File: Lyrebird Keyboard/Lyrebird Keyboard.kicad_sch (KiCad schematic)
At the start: 99 parts, among them IC1 L7915CV, IC2 L78S15CV, IC3 MCP6022-E_SN, IC4 IR2113SPBF, IC5 IR2113SPBF, IC6 LM358DT, IC7 L7805ACD2T-TR, J1 WAV/ENV 4 (MIDI), J10 AC IN 2, J11 240V Out, J12 240 In, J13 Keys 1 to 14, J14 Keys 15 to 28, J15 Keys 29 to 33, J16 Keys 34 to 45, J17 Keys 46 to 59, J18 Keys 60 to 73, J19 Triangle Test, J2 WAV/ENV 3, J20 AMP Out, J21 SUB Out, J22 Square Test, J23 Bias Test Point 2, J24 Bias Test Point 1, J25 Pedals, J3 WAV/ENV 2, J4 WAV/ENV 1, J5 TONE SRC 4, J6 TONE SRC 3, J7 TONE SRC 2, J8 TONE SRC 1, J9 AC IN 1, Q1 BC848, Q2 BC848, Q3 IRFR2905ZTRPBF, Q4 IRFR2905ZTRPBF, Q5 IRFR2905ZTRPBF, Q6 IRFR2905ZTRPBF, U1 DF06S

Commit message: Mainboard Changes
Adjusted mainboard, the longer PCI slots are now instrument slots not wave shaper slots, and slot 4 in the longer is also able to support midi implementation
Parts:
- added C29, C30, C31, C32, C33, C34: T491A225K016AT, T491A, symbol SamacSys_Parts:T491A225K016AT
- J1: value WAV/ENV 4 (MIDI) -> INSTMNT 4 (MIDI)
- J15: value Keys 29 to 33 -> Keys 29 to 36
- J16: value Keys 34 to 45 -> Keys 37 to 45
- J2: value WAV/ENV 3 -> INSTMNT 3
- J3: value WAV/ENV 2 -> INSTMNT 2
- J4: value WAV/ENV 1 -> INSTMNT 1
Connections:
- net +15V: now also J1.A17, J1.A3, J1.B17, J1.B3, J2.A17, J2.A3, J2.B17, J2.B3, J3.A17, J3.A3, J3.B17, J3.B3, J4.A17, J4.A3, J4.B17, J4.B3, J5.A17, J5.A3, J5.B17, J5.B3, J6.A17, J6.A3, J6.B17, J6.B3, J7.A17, J7.A3, J7.B17, J7.B3, J8.A17, J8.A3, J8.B17, J8.B3; no longer J1.A18, J1.A4, J1.B18, J1.B4, J2.A18, J2.A4, J2.B18, J2.B4, J3.A18, J3.A4, J3.B18, J3.B4, J4.A18, J4.A4, J4.B18, J4.B4, J5.A18, J5.A4, J5.B18, J5.B4, J6.A18, J6.A4, J6.B18, J6.B4, J7.A18, J7.A4, J7.B18, J7.B4, J8.A18, J8.A4, J8.B18, J8.B4
- net +30V: now also J1.A1, J1.A15, J1.B1, J1.B15, J2.A1, J2.A15, J2.B1, J2.B15, J3.A1, J3.A15, J3.B1, J3.B15, J4.A1, J4.A15, J4.B1, J4.B15, J5.A1, J5.A15, J5.B1, J5.B15, J6.A1, J6.A15, J6.B1, J6.B15, J7.A1, J7.A15, J7.B1, J7.B15, J8.A1, J8.A15, J8.B1, J8.B15; no longer J1.A16, J1.A2, J1.B16, J1.B2, J2.A16, J2.A2, J2.B16, J2.B2, J3.A16, J3.A2, J3.B16, J3.B2, J4.A16, J4.A2, J4.B16, J4.B2, J5.A16, J5.A2, J5.B16, J5.B2, J6.A16, J6.A2, J6.B16, J6.B2, J7.A16, J7.A2, J7.B16, J7.B2, J8.A16, J8.A2, J8.B16, J8.B2
- net +5V: now also C29.1 (+), C30.1 (+), C31.1 (+), C32.1 (+), C33.1 (+), C34.1 (+)
- net +VED: now also J1.B7, J2.B7, J3.B7, J4.B7, J5.B7, J6.B7, J7.B7, J8.B7; no longer J1.B8, J2.B8, J3.B8, J4.B8, J5.B8, J6.B8, J7.B8, J8.B8
- net +VT: now also J1.A7, J2.A7, J3.A7, J4.A7, J5.A7, J6.A7, J7.A7, J8.A7; no longer J1.A8, J2.A8, J3.A8, J4.A8, J5.A8, J6.A8, J7.A8, J8.A8
- net -15V: now also J1.A19, J1.A5, J1.B19, J1.B5, J2.A19, J2.A5, J2.B19, J2.B5, J3.A19, J3.A5, J3.B19, J3.B5, J4.A19, J4.A5, J4.B19, J4.B5, J5.A19, J5.A5, J5.B19, J5.B5, J6.A19, J6.A5, J6.B19, J6.B5, J7.A19, J7.A5, J7.B19, J7.B5, J8.A19, J8.A5, J8.B19, J8.B5; no longer J1.A20, J1.A6, J1.B20, J1.B6, J2.A20, J2.A6, J2.B20, J2.B6, J3.A20, J3.A6, J3.B20, J3.B6, J4.A20, J4.A6, J4.B20, J4.B6, J5.A20, J5.A6, J5.B20, J5.B6, J6.A20, J6.A6, J6.B20, J6.B6, J7.A20, J7.A6, J7.B20, J7.B6, J8.A20, J8.A6, J8.B20, J8.B6
- net D#35: now also J15.9; no longer J16.5
- net D34: now also J15.8; no longer J16.6
- net E36: now also J15.10; no longer J16.8
- net EXP 1: now also J1.A33, J2.A33, J3.A33, J4.A33, J5.A33, J6.A33, J7.A33, J8.A33; no longer J1.A34, J2.A34, J3.A34, J4.A34, J5.A34, J6.A34, J7.A34, J8.A34
- net EXP 11: now also J1.B39, J2.B39, J3.B39, J4.B39, J5.B39, J6.B39, J7.B39, J8.B39; no longer J1.B40, J2.B40, J3.B40, J4.B40, J5.B40, J6.B40, J7.B40, J8.B40
- net EXP 12: now also J1.B41, J2.B41, J3.B41, J4.B41, J5.B41, J6.B41, J7.B41, J8.B41; no longer J1.B42, J2.B42, J3.B42, J4.B42, J5.B42, J6.B42, J7.B42, J8.B42
- net EXP 13: now also J1.B43, J2.B43, J3.B43, J4.B43, J5.B43, J6.B43, J7.B43, J8.B43; no longer J1.B44, J2.B44, J3.B44, J4.B44, J5.B44, J6.B44, J7.B44, J8.B44
- net EXP 2: now also J1.A35, J2.A35, J3.A35, J4.A35, J5.A35, J6.A35, J7.A35, J8.A35; no longer J1.A36, J2.A36, J3.A36, J4.A36, J5.A36, J6.A36, J7.A36, J8.A36
- net EXP 3: now also J1.A37, J2.A37, J3.A37, J4.A37, J5.A37, J6.A37, J7.A37, J8.A37; no longer J1.A38, J2.A38, J3.A38, J4.A38, J5.A38, J6.A38, J7.A38, J8.A38
- net EXP 4: now also J1.A39, J2.A39, J3.A39, J4.A39, J5.A39, J6.A39, J7.A39, J8.A39; no longer J1.A40, J2.A40, J3.A40, J4.A40, J5.A40, J6.A40, J7.A40, J8.A40
- net EXP 5: now also J1.A41, J2.A41, J3.A41, J4.A41, J5.A41, J6.A41, J7.A41, J8.A41; no longer J1.A42, J2.A42, J3.A42, J4.A42, J5.A42, J6.A42, J7.A42, J8.A42
- net EXP 6: now also J1.A43, J2.A43, J3.A43, J4.A43, J5.A43, J6.A43, J7.A43, J8.A43; no longer J1.A44, J2.A44, J3.A44, J4.A44, J5.A44, J6.A44, J7.A44, J8.A44
- net EXP 7: now also J1.A45, J2.A45, J3.A45, J4.A45, J5.A45, J6.A45, J7.A45, J8.A45; no longer J1.A46, J2.A46, J3.A46, J4.A46, J5.A46, J6.A46, J7.A46, J8.A46
- net EXP10: now also J1.B37, J2.B37, J3.B37, J4.B37, J5.B37, J6.B37, J7.B37, J8.B37; no longer J1.B38, J2.B38, J3.B38, J4.B38, J5.B38, J6.B38, J7.B38, J8.B38
- net EXP8: now also J1.B33, J2.B33, J3.B33, J4.B33, J5.B33, J6.B33, J7.B33, J8.B33; no longer J1.B34, J2.B34, J3.B34, J4.B34, J5.B34, J6.B34, J7.B34, J8.B34
- net EXP9: now also J1.B35, J2.B35, J3.B35, J4.B35, J5.B35, J6.B35, J7.B35, J8.B35; no longer J1.B36, J2.B36, J3.B36, J4.B36, J5.B36, J6.B36, J7.B36, J8.B36
- net GND: now also J1.A10, J1.A12, J1.A14, J1.A16, J1.A18, J1.A2, J1.A20, J1.A22, J1.A24, J1.A26, J1.A28, J1.A30, J1.A32, J1.A34, J1.A36, J1.A38, J1.A4, J1.A40, J1.A42, J1.A44, J1.A46, J1.A6, J1.A8, J1.B10, J1.B12, J1.B14, J1.B16, J1.B18, J1.B2, J1.B20, J1.B22, J1.B24, J1.B26, J1.B28, J1.B30, J1.B32, J1.B34, J1.B36, J1.B38, J1.B4, J1.B40, J1.B42, J1.B44, J1.B6, J1.B8, J2.A10, J2.A12, J2.A14, J2.A16, J2.A18, J2.A2, J2.A20, J2.A22, J2.A24, J2.A26, J2.A28, J2.A30, J2.A32, J2.A34, J2.A36, J2.A38, J2.A4, J2.A40, J2.A42, J2.A44, J2.A46, J2.A6, J2.A8, J2.B10, J2.B12, J2.B14, J2.B16, J2.B18, J2.B2, J2.B20, J2.B22, J2.B24, J2.B26, J2.B28, J2.B30, J2.B32, J2.B34, J2.B36, J2.B38, J2.B4, J2.B40, J2.B42, J2.B44, J2.B6, J2.B8, J3.A10, J3.A12, J3.A14, J3.A16, J3.A18, J3.A2, J3.A20, J3.A22, J3.A24, J3.A26, J3.A28, J3.A30, J3.A32, J3.A34, J3.A36, J3.A38, J3.A4, J3.A40, J3.A42, J3.A44, J3.A46, J3.A6, J3.A8, J3.B10, J3.B12, J3.B14, J3.B16, J3.B18, J3.B2, J3.B20, J3.B22, J3.B24, J3.B26, J3.B28, J3.B30, J3.B32, J3.B34, J3.B36, J3.B38, J3.B4, J3.B40, J3.B42, J3.B44, J3.B6, J3.B8, J4.A10, J4.A12, J4.A14, J4.A16, J4.A18, J4.A2, J4.A20, J4.A22, J4.A24, J4.A26, J4.A28, J4.A30, J4.A32, J4.A34, J4.A36, J4.A38, J4.A4, J4.A40, J4.A42, J4.A44, J4.A46, J4.A6, J4.A8, J4.B10, J4.B12, J4.B14, J4.B16, J4.B18, J4.B2, J4.B20, J4.B22, J4.B24, J4.B26, J4.B28, J4.B30, J4.B32, J4.B34, J4.B36, J4.B38, J4.B4, J4.B40, J4.B42, J4.B44, J4.B6, J4.B8, J5.A10, J5.A12, J5.A14, J5.A16, J5.A18, J5.A2, J5.A20, J5.A22, J5.A24, J5.A26, J5.A28, J5.A30, J5.A32, J5.A34, J5.A36, J5.A38, J5.A4, J5.A40, J5.A42, J5.A44, J5.A46, J5.A48, J5.A6, J5.A8, J5.B10, J5.B12, J5.B14, J5.B16, J5.B18, J5.B2, J5.B20, J5.B22, J5.B24, J5.B26, J5.B28, J5.B30, J5.B32, J5.B34, J5.B36, J5.B38, J5.B4, J5.B40, J5.B42, J5.B44, J5.B46, J5.B48, J5.B6, J5.B8, J6.A10, J6.A12, J6.A14, J6.A16, J6.A18, J6.A2, J6.A20, J6.A22, J6.A24, J6.A26, J6.A28, J6.A30, J6.A32, J6.A34, J6.A36, J6.A38, J6.A4, J6.A40, J6.A42, J6.A44, J6.A46, J6.A48, J6.A6, J6.A8, J6.B10, J6.B12, J6.B14, J6.B16, J6.B18, J6.B2, J6.B20, J6.B22, J6.B24, J6.B26, J6.B28, J6.B30, J6.B32, J6.B34, J6.B36, J6.B38, J6.B4, J6.B40, J6.B42, J6.B44, J6.B46, J6.B48, J6.B6, J6.B8, J7.A10, J7.A12, J7.A14, J7.A16, J7.A18, J7.A2, J7.A20, J7.A22, J7.A24, J7.A26, J7.A28, J7.A30, J7.A32, J7.A34, J7.A36, J7.A38, J7.A4, J7.A40, J7.A42, J7.A44, J7.A46, J7.A48, J7.A6, J7.A8, J7.B10, J7.B12, J7.B14, J7.B16, J7.B18, J7.B2, J7.B20, J7.B22, J7.B24, J7.B26, J7.B28, J7.B30, J7.B32, J7.B34, J7.B36, J7.B38, J7.B4, J7.B40, J7.B42, J7.B44, J7.B46, J7.B48, J7.B6, J7.B8, J8.A10, J8.A12, J8.A14, J8.A16, J8.A18, J8.A2, J8.A20, J8.A22, J8.A24, J8.A26, J8.A28, J8.A30, J8.A32, J8.A34, J8.A36, J8.A38, J8.A4, J8.A40, J8.A42, J8.A44, J8.A46, J8.A48, J8.A6, J8.A8, J8.B10, J8.B12, J8.B14, J8.B16, J8.B18, J8.B2, J8.B20, J8.B22, J8.B24, J8.B26, J8.B28, J8.B30, J8.B32, J8.B34, J8.B36, J8.B38, J8.B4, J8.B40, J8.B42, J8.B44, J8.B46, J8.B48, J8.B6, J8.B8, C29.2 (-), C30.2 (-), C31.2 (-), C32.2 (-), C33.2 (-), C34.2 (-); no longer J1.A1, J1.A11, J1.A13, J1.A15, J1.A17, J1.A19, J1.A21, J1.A23, J1.A25, J1.A27, J1.A29, J1.A3, J1.A31, J1.A33, J1.A35, J1.A37, J1.A39, J1.A41, J1.A43, J1.A45, J1.A5, J1.A7, J1.A9, J1.B1, J1.B11, J1.B13, J1.B15, J1.B17, J1.B19, J1.B21, J1.B23, J1.B25, J1.B27, J1.B29, J1.B3, J1.B31, J1.B33, J1.B35, J1.B37, J1.B39, J1.B41, J1.B43, J1.B45, J1.B5, J1.B7, J1.B9, J2.A1, J2.A11, J2.A13, J2.A15, J2.A17, J2.A19, J2.A21, J2.A23, J2.A25, J2.A27, J2.A29, J2.A3, J2.A31, J2.A33, J2.A35, J2.A37, J2.A39, J2.A41, J2.A43, J2.A45, J2.A5, J2.A7, J2.A9, J2.B1, J2.B11, J2.B13, J2.B15, J2.B17, J2.B19, J2.B21, J2.B23, J2.B25, J2.B27, J2.B29, J2.B3, J2.B31, J2.B33, J2.B35, J2.B37, J2.B39, J2.B41, J2.B43, J2.B45, J2.B5, J2.B7, J2.B9, J3.A1, J3.A11, J3.A13, J3.A15, J3.A17, J3.A19, J3.A21, J3.A23, J3.A25, J3.A27, J3.A29, J3.A3, J3.A31, J3.A33, J3.A35, J3.A37, J3.A39, J3.A41, J3.A43, J3.A45, J3.A5, J3.A7, J3.A9, J3.B1, J3.B11, J3.B13, J3.B15, J3.B17, J3.B19, J3.B21, J3.B23, J3.B25, J3.B27, J3.B29, J3.B3, J3.B31, J3.B33, J3.B35, J3.B37, J3.B39, J3.B41, J3.B43, J3.B45, J3.B5, J3.B7, J3.B9, J4.A1, J4.A11, J4.A13, J4.A15, J4.A17, J4.A19, J4.A21, J4.A23, J4.A25, J4.A27, J4.A29, J4.A3, J4.A31, J4.A33, J4.A35, J4.A37, J4.A39, J4.A41, J4.A43, J4.A45, J4.A5, J4.A7, J4.A9, J4.B1, J4.B11, J4.B13, J4.B15, J4.B17, J4.B19, J4.B21, J4.B23, J4.B25, J4.B27, J4.B29, J4.B3, J4.B31, J4.B33, J4.B35, J4.B37, J4.B39, J4.B41, J4.B43, J4.B45, J4.B5, J4.B7, J4.B9, J5.A1, J5.A11, J5.A13, J5.A15, J5.A17, J5.A19, J5.A21, J5.A23, J5.A25, J5.A27, J5.A29, J5.A3, J5.A31, J5.A33, J5.A35, J5.A37, J5.A39, J5.A41, J5.A43, J5.A45, J5.A47, J5.A49, J5.A5, J5.A7, J5.A9, J5.B1, J5.B11, J5.B13, J5.B15, J5.B17, J5.B19, J5.B21, J5.B23, J5.B25, J5.B27, J5.B29, J5.B3, J5.B31, J5.B33, J5.B35, J5.B37, J5.B39, J5.B41, J5.B43, J5.B45, J5.B47, J5.B49, J5.B5, J5.B7, J5.B9, J6.A1, J6.A11, J6.A13, J6.A15, J6.A17, J6.A19, J6.A21, J6.A23, J6.A25, J6.A27, J6.A29, J6.A3, J6.A31, J6.A33, J6.A35, J6.A37, J6.A39, J6.A41, J6.A43, J6.A45, J6.A47, J6.A49, J6.A5, J6.A7, J6.A9, J6.B1, J6.B11, J6.B13, J6.B15, J6.B17, J6.B19, J6.B21, J6.B23, J6.B25, J6.B27, J6.B29, J6.B3, J6.B31, J6.B33, J6.B35, J6.B37, J6.B39, J6.B41, J6.B43, J6.B45, J6.B47, J6.B49, J6.B5, J6.B7, J6.B9, J7.A1, J7.A11, J7.A13, J7.A15, J7.A17, J7.A19, J7.A21, J7.A23, J7.A25, J7.A27, J7.A29, J7.A3, J7.A31, J7.A33, J7.A35, J7.A37, J7.A39, J7.A41, J7.A43, J7.A45, J7.A47, J7.A49, J7.A5, J7.A7, J7.A9, J7.B1, J7.B11, J7.B13, J7.B15, J7.B17, J7.B19, J7.B21, J7.B23, J7.B25, J7.B27, J7.B29, J7.B3, J7.B31, J7.B33, J7.B35, J7.B37, J7.B39, J7.B41, J7.B43, J7.B45, J7.B47, J7.B49, J7.B5, J7.B7, J7.B9, J8.A1, J8.A11, J8.A13, J8.A15, J8.A17, J8.A19, J8.A21, J8.A23, J8.A25, J8.A27, J8.A29, J8.A3, J8.A31, J8.A33, J8.A35, J8.A37, J8.A39, J8.A41, J8.A43, J8.A45, J8.A47, J8.A49, J8.A5, J8.A7, J8.A9, J8.B1, J8.B11, J8.B13, J8.B15, J8.B17, J8.B19, J8.B21, J8.B23, J8.B25, J8.B27, J8.B29, J8.B3, J8.B31, J8.B33, J8.B35, J8.B37, J8.B39, J8.B41, J8.B43, J8.B45, J8.B47, J8.B49, J8.B5, J8.B7, J8.B9
- net LINE OUT: now also J1.B13, J2.B13, J3.B13, J4.B13, J5.B13, J6.B13, J7.B13, J8.B13; no longer J1.B14, J2.B14, J3.B14, J4.B14, J5.B14, J6.B14, J7.B14, J8.B14
- net SELECT 1: now also J1.B45, J2.B45, J3.B45, J4.B45, J5.B45, J6.B45, J7.B45, J8.B45; no longer J5.B46, J6.B46, J7.B46, J8.B46
- net SELECT 2: now also J5.B47, J6.B47, J7.B47, J8.B47; no longer J5.B48, J6.B48, J7.B48, J8.B48
- net SELECT 3: now also J5.B49, J6.B49, J7.B49, J8.B49; no longer J5.A48, J6.A48, J7.A48, J8.A48
- net SELECT 4: now also J5.A47, J6.A47, J7.A47, J8.A47; no longer J1.A10, J2.A10, J3.A10, J4.A10, J5.A10, J6.A10, J7.A10, J8.A10
- net SELECT 5: now also J5.A49, J6.A49, J7.A49, J8.A49; no longer J1.A12, J2.A12, J3.A12, J4.A12, J5.A12, J6.A12, J7.A12, J8.A12
- net SELECT 6: now also J1.A9, J2.A9, J3.A9, J4.A9, J5.A9, J6.A9, J7.A9, J8.A9; no longer J1.A14, J2.A14, J3.A14, J4.A14, J5.A14, J6.A14, J7.A14, J8.A14
- net SOFT: now also J1.B11, J2.B11, J3.B11, J4.B11, J5.B11, J6.B11, J7.B11, J8.B11; no longer J1.B12, J2.B12, J3.B12, J4.B12, J5.B12, J6.B12, J7.B12, J8.B12
- net SUSTAIN: now also J1.B9, J2.B9, J3.B9, J4.B9, J5.B9, J6.B9, J7.B9, J8.B9; no longer J1.B10, J2.B10, J3.B10, J4.B10, J5.B10, J6.B10, J7.B10, J8.B10
- net TONE 1: now also J1.A21, J2.A21, J3.A21, J4.A21, J5.A21, J6.A21, J7.A21, J8.A21; no longer J1.A22, J2.A22, J3.A22, J4.A22, J5.A22, J6.A22, J7.A22, J8.A22
- net TONE 10: now also J1.B27, J2.B27, J3.B27, J4.B27, J5.B27, J6.B27, J7.B27, J8.B27; no longer J1.B28, J2.B28, J3.B28, J4.B28, J5.B28, J6.B28, J7.B28, J8.B28
- net TONE 11: now also J1.B29, J2.B29, J3.B29, J4.B29, J5.B29, J6.B29, J7.B29, J8.B29; no longer J1.B30, J2.B30, J3.B30, J4.B30, J5.B30, J6.B30, J7.B30, J8.B30
- net TONE 12: now also J1.B31, J2.B31, J3.B31, J4.B31, J5.B31, J6.B31, J7.B31, J8.B31; no longer J1.B32, J2.B32, J3.B32, J4.B32, J5.B32, J6.B32, J7.B32, J8.B32
- net TONE 2: now also J1.A23, J2.A23, J3.A23, J4.A23, J5.A23, J6.A23, J7.A23, J8.A23; no longer J1.A24, J2.A24, J3.A24, J4.A24, J5.A24, J6.A24, J7.A24, J8.A24
- net TONE 3: now also J1.A25, J2.A25, J3.A25, J4.A25, J5.A25, J6.A25, J7.A25, J8.A25; no longer J1.A26, J2.A26, J3.A26, J4.A26, J5.A26, J6.A26, J7.A26, J8.A26
- net TONE 4: now also J1.A27, J2.A27, J3.A27, J4.A27, J5.A27, J6.A27, J7.A27, J8.A27; no longer J1.A28, J2.A28, J3.A28, J4.A28, J5.A28, J6.A28, J7.A28, J8.A28
- net TONE 5: now also J1.A29, J2.A29, J3.A29, J4.A29, J5.A29, J6.A29, J7.A29, J8.A29; no longer J1.A30, J2.A30, J3.A30, J4.A30, J5.A30, J6.A30, J7.A30, J8.A30
- net TONE 6: now also J1.A31, J2.A31, J3.A31, J4.A31, J5.A31, J6.A31, J7.A31, J8.A31; no longer J1.A32, J2.A32, J3.A32, J4.A32, J5.A32, J6.A32, J7.A32, J8.A32
- net TONE 7: now also J1.B21, J2.B21, J3.B21, J4.B21, J5.B21, J6.B21, J7.B21, J8.B21; no longer J1.B22, J2.B22, J3.B22, J4.B22, J5.B22, J6.B22, J7.B22, J8.B22
- net TONE 8: now also J1.B23, J2.B23, J3.B23, J4.B23, J5.B23, J6.B23, J7.B23, J8.B23; no longer J1.B24, J2.B24, J3.B24, J4.B24, J5.B24, J6.B24, J7.B24, J8.B24
- net TONE 9: now also J1.B25, J2.B25, J3.B25, J4.B25, J5.B25, J6.B25, J7.B25, J8.B25; no longer J1.B26, J2.B26, J3.B26, J4.B26, J5.B26, J6.B26, J7.B26, J8.B26
- new net SELECT 7: J1.A11, J2.A11, J3.A11, J4.A11, J5.A11, J6.A11, J7.A11, J8.A11
- new net SELECT 8: J1.A13, J2.A13, J3.A13, J4.A13, J5.A13, J6.A13, J7.A13, J8.A13
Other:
- moved on the sheet: J1

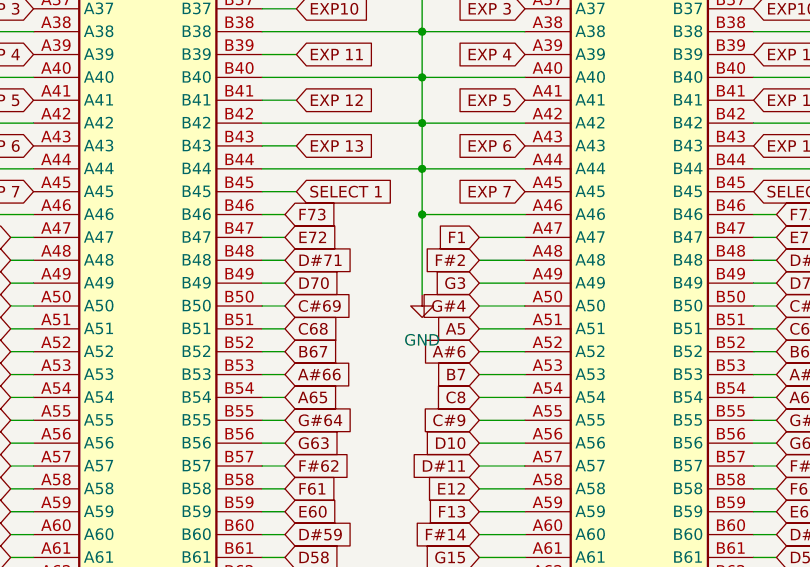
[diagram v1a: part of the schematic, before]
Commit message: Piano Board Layout
Started doing circuit that creates the piano sound.
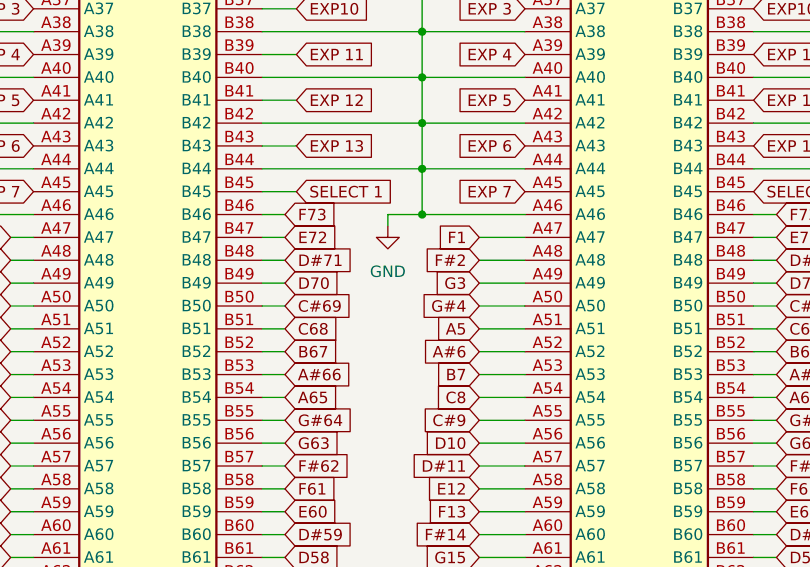
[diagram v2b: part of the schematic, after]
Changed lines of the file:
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@@
     (stroke (width 0) (type default))
   )
-  (wire (pts (xy 529.59 148.59) (xy 529.59 157.48))
+  (wire (pts (xy 525.78 148.59) (xy 525.78 149.86))
     (stroke (width 0) (type default))
   )
@@
     (stroke (width 0) (type default))
   )
+  (wire (pts (xy 525.78 148.59) (xy 529.59 148.59))
+    (stroke (width 0) (type default))
+  )
   (wire (pts (xy 483.87 186.69) (xy 486.41 186.69))
     (stroke (width 0) (type default))
@@
     )
   )
-  (symbol (lib_id "power:GND") (at 529.59 157.48 0) (unit 1)
+  (symbol (lib_id "power:GND") (at 525.78 149.86 0) (unit 1)
     (in_bom yes) (on_board yes) (dnp no) (fields_autoplaced)
-    (property "Reference" "#PWR036" (at 529.59 163.83 0)
+    (property "Reference" "#PWR036" (at 525.78 156.21 0)
       (effects (font (size 1.27 1.27)) hide)
     )
-    (property "Value" "GND" (at 529.59 162.56 0)
+    (property "Value" "GND" (at 525.78 154.94 0)
       (effects (font (size 1.27 1.27)))
     )
-    (property "Footprint" "" (at 529.59 157.48 0)
+    (property "Footprint" "" (at 525.78 149.86 0)
       (effects (font (size 1.27 1.27)) hide)
     )
-    (property "Datasheet" "" (at 529.59 157.48 0)
+    (property "Datasheet" "" (at 525.78 149.86 0)
       (effects (font (size 1.27 1.27)) hide)
     )

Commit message: Design Changes
Fix a number of symbol issues, and connection faults
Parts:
- removed C19: 1nF, Capacitor_SMD:C_1206_3216Metric, symbol Device:C_Small
- removed C19: 68nF, Capacitor_SMD:C_1206_3216Metric, symbol Device:C_Small
- removed IC3: MCP6022-E_SN, SamacSys_Parts:SOIC127P600X175-8N, symbol SamacSys_Parts:MCP6022-E_SN
- removed IC6: LM358DT, SamacSys_Parts:SOIC127P600X175-8N, symbol SamacSys_Parts:LM358DT
- removed R12: 10k, Resistor_SMD:R_1206_3216Metric, symbol Device:R
- removed R12: 5k1, Resistor_SMD:R_1206_3216Metric, symbol Device:R
- removed R17: CT-9EW104, SamacSys_Parts:CT9EW104, symbol SamacSys_Parts:CT-9EW104
- removed VR1: 3362P-1-102LF, SamacSys_Parts:3362P_1, symbol SamacSys_Parts:3362P-1-102LF
- removed VR2, VR3, VR4: T73YP103KT20, SamacSys_Parts:T73YP103KT20, symbol SamacSys_Parts:T73YP103KT20
- added C19: 1nF, Capacitor_SMD:C_1206_3216Metric, symbol Device:C_Small
- added C19: 68nF, Capacitor_SMD:C_1206_3216Metric, symbol Device:C_Small
- added R12: 10k, Resistor_SMD:R_1206_3216Metric, symbol Device:R
- added R12: 5k1, Resistor_SMD:R_1206_3216Metric, symbol Device:R
- added U2: LM358, SamacSys_Parts:SOIC127P600X175-8N, symbol Amplifier_Operational:LM358
- added U3: ~, SamacSys_Parts:SOIC127P600X175-8N, symbol SamacSys_Parts:MCP6022-PF
- added VR1: 3362P-1-102LF, SamacSys_Parts:3362P_1, symbol SparkFun-Resistors:TRIMPOT-PTH-10MM-KNOB-1_2W-10%
- added VR2, VR3, VR4: T73YP103KT20, SamacSys_Parts:T73YP103KT20, symbol SparkFun-Resistors:TRIMPOT-PTH-10MM-KNOB-1_2W-10%
- added VR5: CT-9EW104, SamacSys_Parts:CT9EW104, symbol SparkFun-Resistors:TRIMPOT-PTH-10MM-KNOB-1_2W-10%
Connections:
- net +5V: now also U2.8 (V+), U3.8 (Vdd), VR2.3 (CW), VR4.3 (CW)
- net +VED: now also VR1.2 (WIPER)
- net GND: now also C19.1, U2.2 (-), U2.4 (V-), U2.5 (+), U3.4 (Vss), VR2.1 (CCW), VR4.1 (CCW)
- net LINE OUT: now also VR3.3 (CW)
- net PCM LNE OUT: now also U3.1
- net PCM SUB OUT: now also U3.7
- net SUB IN: now also J23.1 (Pin_1), R12.2, VR2.2 (WIPER), VR3.2 (WIPER)
- net TRI WAVE OUT: now also C19.2, U2.7, U3.3 (+), U3.5 (+)
- net at R12.1: now also J22.1 (Pin_1), Z1.2 (A), R12.2, VR5.1 (CCW); no longer R12.2
- net at J24.1 (Pin_1): now also U3.2 (-), VR3.1 (CCW), VR4.2 (WIPER)
- net at R2.2: now also VR1.3 (CW)
- net at C7.1 (+): now also VR1.1 (CCW)
- removed net SQUARE: J22.1 (Pin_1), R12.2, Z1.2 (A)
- new net: C19.2, R12.1, U3.6 (-)
- new net: C19.1, U2.6 (-), VR5.2 (WIPER)
- new net: R12.1, U2.1
- new net: R12.2, R12.2, U2.3 (+)
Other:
- moved on the sheet: C29, C31, IC5, J24, Q1, R12, R17, Z1, Z2
